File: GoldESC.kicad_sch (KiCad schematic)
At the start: 5 parts, among them U20 PSMN1R0-30YLDX

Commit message: Added fets and drivers, initial critical components selected
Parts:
- removed IC?: ESP32-S2, QFN56_ESP32_7X7_EXP, symbol AlfredoSymbols:ESP32-S2
- removed U20: PSMN1R0-30YLDX, Package_TO_SOT_SMD:LFPAK56, symbol AlfredoSymbols:PSMN1R0-30YLDX
- removed U?: LM5111-1M/NOPB, symbol AlfredoSymbols:LM5111-1M/NOPB
- removed U?: AD8417, symbol Amplifier_Current:AD8417
- removed U?: A4950E, Package_SO:SOIC-8-1EP_3.9x4.9mm_P1.27mm_EP2.41x3.3mm, symbol Driver_Motor:A4950E
- added C4: 470nF?/16V?, symbol Device:C_Small
- added C5, C6: ?uF/?V, symbol Device:C_Small
- added C? (x5): 2.2uF, Capacitor_SMD:C_0603_1608Metric, symbol Device:C
- added C? (x2): 100nF, Capacitor_SMD:C_0603_1608Metric, symbol Device:C
- added D1, D2, D3: S1M-13, Diode_SMD:D_SMA, symbol Diode:US1M
- added D?: GREEN, LED_THT:LED_D3.0mm, symbol Device:LED
- added D?: BLUE, LED_THT:LED_D3.0mm, symbol Device:LED
- added D?: ZMM3V3, Diode_SMD:D_MiniMELF, symbol Device:D_Zener
- added D?: RED, LED_THT:LED_D3.0mm, symbol Device:LED
- added J1: PhaseA, symbol Connector_Generic:Conn_01x01
- added J2: PhaseB, symbol Connector_Generic:Conn_01x01
- added J3: PhaseC, symbol Connector_Generic:Conn_01x01
- added J?: Conn_ESC_2A, Connector_PinSocket_2.54mm:PinSocket_1x11_P2.54mm_Vertical, symbol Connector_Generic:Conn_01x11
- added J? (x3): Conn_MCU_B, Connector_PinSocket_2.54mm:PinSocket_1x11_P2.54mm_Vertical, symbol Connector_Generic:Conn_01x11
- added J? (x4): Conn_01x06, Connector_PinSocket_2.54mm:PinSocket_1x06_P2.54mm_Vertical, symbol Connector_Generic:Conn_01x06
- added J?: Conn_MCU_A, Connector_PinSocket_2.54mm:PinSocket_1x11_P2.54mm_Vertical, symbol Connector_Generic:Conn_01x11
- added J?: Conn_ESC_1A, Connector_PinSocket_2.54mm:PinSocket_1x11_P2.54mm_Vertical, symbol Connector_Generic:Conn_01x11
- added R? (x4): 2K2, Resistor_SMD:R_0603_1608Metric, symbol Device:R
- added R? (x3): 3.3K, Resistor_SMD:R_0805_2012Metric, symbol Device:R
- added R? (x2): 22R, Resistor_SMD:R_0603_1608Metric, symbol Device:R
- added R? (x2): 10K, Resistor_SMD:R_0603_1608Metric, symbol Device:R
- added R?: 15K, Resistor_SMD:R_0603_1608Metric, symbol Device:R
- added R?: 10K RTC, Resistor_SMD:R_0603_1608Metric, symbol Device:R
- added U2: DRV8300NIPWR, Package_SO:TSSOP-20_4.4x6.5mm_P0.65mm, symbol AlfredoSymbols:DRV8300NIPWR
- added U3: MCP2551-I-SN, Package_SO:SOIC-8_3.9x4.9mm_P1.27mm, symbol Interface_CAN_LIN:MCP2551-I-SN
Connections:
- new net: D?.2 (A), R?.1 (x3)
- new net: C6.1, D3.1 (K), U2.14 (BSTC)
- new net: D1.2 (A), D2.2 (A), D3.2 (A), U2.7 (GVDD)
- new net: J?.5 (Pin_5), R?.2
- new net: C4.1, D1.1 (K), U2.20 (BSTA)
- new net: C5.1, D2.1 (K), U2.17 (BSTB)
- new net: J?.4 (Pin_4), R?.2
- new net +3V3: C?.1, C?.1, C?.1, C?.1, C?.1, J?.1 (Pin_1), J?.1 (Pin_1), J?.7 (Pin_7), J?.7 (Pin_7), J?.7 (Pin_7), R?.1, R?.1, R?.1, R?.1, R?.2, R?.2
- new net ADC_TEMP: J?.1 (Pin_1), J?.1 (Pin_1), J?.1 (Pin_1)
- new net D_CS: J?.2 (Pin_2)
- new net D_MISO: J?.4 (Pin_4)
- new net D_MOSI: J?.3 (Pin_3)
- new net D_SCK: J?.5 (Pin_5)
- new net EN_GATE: J?.8 (Pin_8), J?.8 (Pin_8), J?.8 (Pin_8)
- new net FAULT: J?.1 (Pin_1), J?.1 (Pin_1), J?.1 (Pin_1)
- new net FET_TEMP: R?.1, R?.2
- new net GE-Fets-A/GHx: U2.19 (GHA)
- new net GE-Fets-A/GLx: U2.11 (GLA)
- new net GE-Fets-A/PHx: J1.1 (Pin_1)
- new net GE-Fets-A/SHx: C4.2, U2.18 (SHA)
- new net GE-Fets-B/GHx: U2.16 (GHB)
- new net GE-Fets-B/GLx: U2.10 (GLB)
- new net GE-Fets-B/PHx: J2.1 (Pin_1)
- new net GE-Fets-B/SHx: C5.2, U2.15 (SHB)
- new net GE-Fets-C/GHx: U2.13 (GHC)
- new net GE-Fets-C/GLx: U2.9 (GLC)
- new net GE-Fets-C/PHx: J3.1 (Pin_1)
- new net GE-Fets-C/SHx: C6.2, U2.12 (SHC)
- new net GND: C?.1, C?.2, C?.2, C?.2, C?.2, C?.2, C?.2, D?.1 (K), D?.1 (K), D?.1 (K), D?.2 (A), J?.3 (Pin_3), J?.6 (Pin_6), J?.6 (Pin_6), J?.6 (Pin_6), J?.6 (Pin_6), J?.6 (Pin_6), J?.6 (Pin_6), R?.1, R?.2, U2.8 (GND)
- new net HALL_1: J?.3 (Pin_3), R?.2
- new net HALL_2: J?.4 (Pin_4), R?.2
- new net HALL_3: J?.5 (Pin_5), R?.2
- new net INH_A: J?.7 (Pin_7), J?.7 (Pin_7), J?.7 (Pin_7)
- new net INH_B: J?.5 (Pin_5), J?.5 (Pin_5), J?.5 (Pin_5)
- new net INH_C: J?.3 (Pin_3), J?.3 (Pin_3), J?.3 (Pin_3)
- new net INL_A: J?.6 (Pin_6), J?.6 (Pin_6), J?.6 (Pin_6)
- new net INL_B: J?.4 (Pin_4), J?.4 (Pin_4), J?.4 (Pin_4)
- new net INL_C: J?.2 (Pin_2), J?.2 (Pin_2), J?.2 (Pin_2)
- new net RX: J?.4 (Pin_4)
- new net S1_CS: J?.2 (Pin_2)
- new net S1_MISO_AE2: J?.1 (Pin_1), J?.4 (Pin_4)
- new net S1_MOSI: J?.5 (Pin_5)
- new net S1_SCK_AE1: J?.3 (Pin_3), J?.6 (Pin_6)
- new net S3_CS: J?.2 (Pin_2), J?.2 (Pin_2)
- new net S3_MISO: J?.4 (Pin_4), J?.4 (Pin_4)
- new net S3_MOSI: J?.3 (Pin_3), J?.3 (Pin_3)
- new net S3_SCK: J?.5 (Pin_5), J?.5 (Pin_5)
- new net SERVO: J?.1 (Pin_1)
- new net SH_A: J?.11 (Pin_11), J?.11 (Pin_11), J?.11 (Pin_11)
- new net SH_B: J?.10 (Pin_10), J?.10 (Pin_10), J?.10 (Pin_10)
- new net SH_C: J?.9 (Pin_9), J?.9 (Pin_9), J?.9 (Pin_9)
- new net SWCLK: J?.3 (Pin_3)
- new net SWDIO: J?.2 (Pin_2)
- new net TEMP_MOTOR: C?.2, J?.2 (Pin_2), R?.1
- new net TX: J?.5 (Pin_5)
- new net USB_DM: R?.1
- new net USB_DP: R?.1
- new net VDD: J?.8 (Pin_8), J?.8 (Pin_8), J?.8 (Pin_8), R?.2
- new net sCUR_A: J?.9 (Pin_9), J?.9 (Pin_9), J?.9 (Pin_9)
- new net sCUR_B: J?.10 (Pin_10), J?.10 (Pin_10), J?.10 (Pin_10)
- new net sCUR_C: J?.11 (Pin_11), J?.11 (Pin_11), J?.11 (Pin_11)
- new net sVLT_VDD: C?.1, D?.1 (K), R?.1, R?.2
- no-connect marks 0 -> 1
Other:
- added sheet GE-ESP32-S2 (GE-ESP32-S2.kicad_sch)
- added sheet GE-Fets-A (GE-Fets.kicad_sch)
- added sheet GE-Fets-B (GE-Fets.kicad_sch)
- added sheet GE-Fets-C (GE-Fets.kicad_sch)
- added sheet GE-Regs (GE-Regs.kicad_sch)
- note added: "Ref-map: 1 -39 -> fets/driver 40-69 -> Regs 70-89 -> ESP32 90-99 -> CAN"
- note added: "for VDDA"
- note added: "place next to VDD pins"

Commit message: switched to stm32
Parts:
- removed C? (x5): 2.2uF, Capacitor_SMD:C_0603_1608Metric, symbol Device:C
- removed J?: Conn_ESC_2A, Connector_PinSocket_2.54mm:PinSocket_1x11_P2.54mm_Vertical, symbol Connector_Generic:Conn_01x11
- removed J? (x3): Conn_MCU_B, Connector_PinSocket_2.54mm:PinSocket_1x11_P2.54mm_Vertical, symbol Connector_Generic:Conn_01x11
- removed J? (x4): Conn_01x06, Connector_PinSocket_2.54mm:PinSocket_1x06_P2.54mm_Vertical, symbol Connector_Generic:Conn_01x06
- removed J?: Conn_MCU_A, Connector_PinSocket_2.54mm:PinSocket_1x11_P2.54mm_Vertical, symbol Connector_Generic:Conn_01x11
- removed J?: Conn_ESC_1A, Connector_PinSocket_2.54mm:PinSocket_1x11_P2.54mm_Vertical, symbol Connector_Generic:Conn_01x11
- C5, C6: value ?uF/?V -> 470nF?/16V?
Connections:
- net GE-STM32F103/INHA: now reaches U2.1 (INHA)
- net GE-STM32F103/INHB: now reaches U2.2 (INHB)
- net GE-STM32F103/INHC: now reaches U2.3 (INHC)
- net GE-STM32F103/INLA: now reaches U2.4 (INLA)
- net GE-STM32F103/INLB: now reaches U2.5 (INLB)
- net GE-STM32F103/INLC: now reaches U2.6 (INLC)
- net FET_TEMP renamed TEMP_FETS
- no-connect marks 1 -> 0
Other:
- removed sheet GE-ESP32-S2
- added sheet GE-STM32F103 (GE-STM32F103.kicad_sch)
- note removed: "for VDDA"
- note removed: "place next to VDD pins"
- moved on the sheet: C?, D?, R?

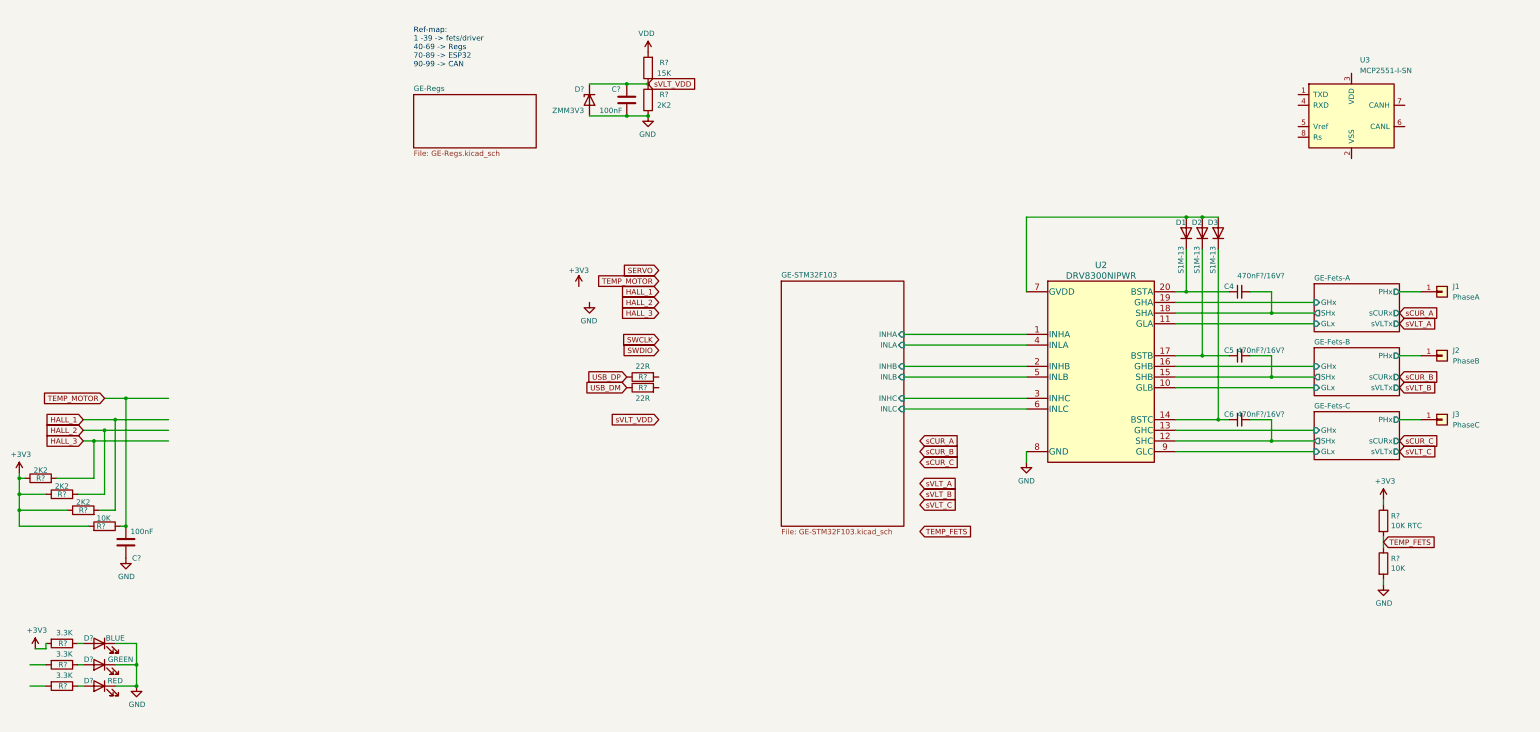
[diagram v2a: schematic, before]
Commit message: moved the Dsub off-board, most of initial layout routed
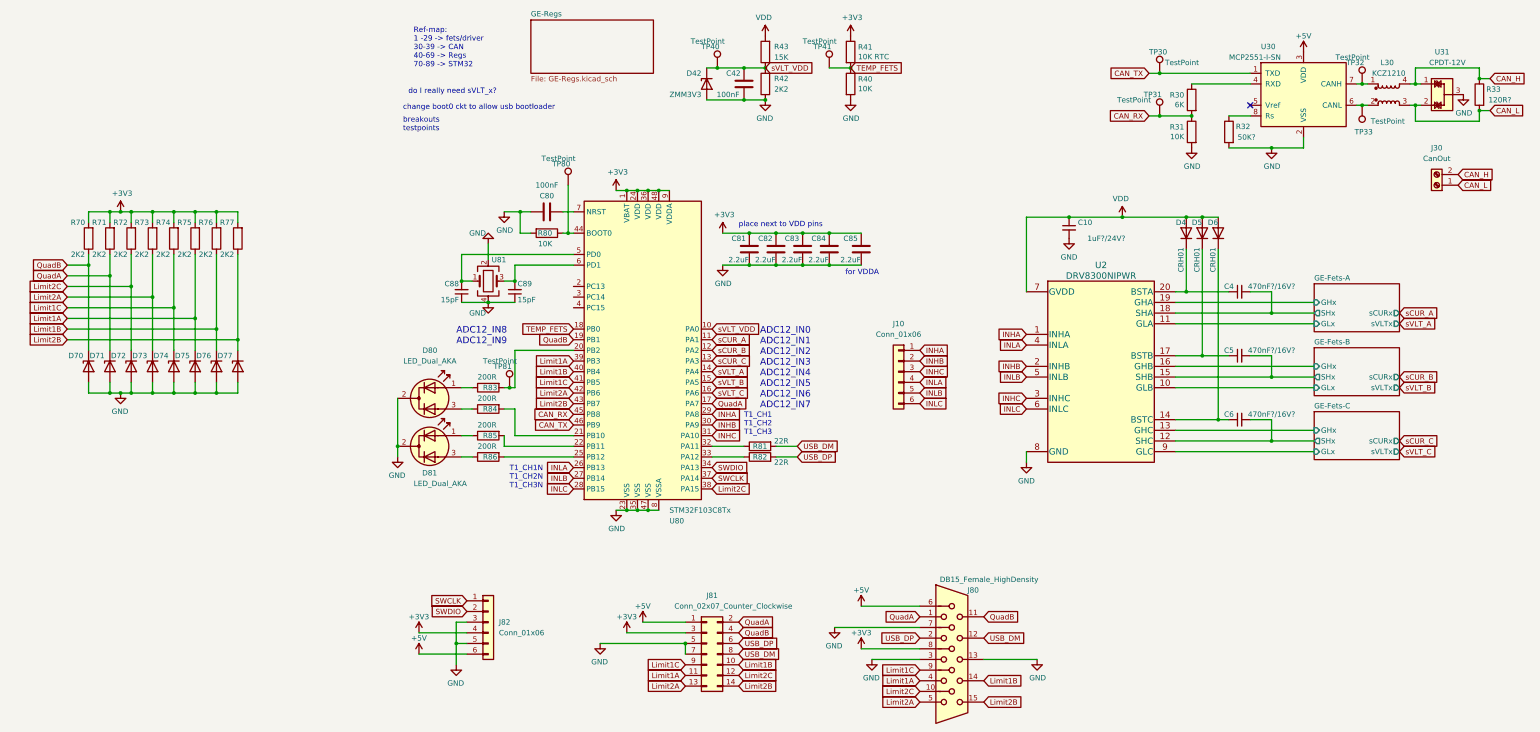
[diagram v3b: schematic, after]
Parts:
- removed C?: 100nF, Capacitor_SMD:C_0603_1608Metric, symbol Device:C
- removed D?: GREEN, LED_THT:LED_D3.0mm, symbol Device:LED
- removed D?: BLUE, LED_THT:LED_D3.0mm, symbol Device:LED
- removed D?: RED, LED_THT:LED_D3.0mm, symbol Device:LED
- removed J1: PhaseA, symbol Connector_Generic:Conn_01x01
- removed J2: PhaseB, symbol Connector_Generic:Conn_01x01
- removed J3: PhaseC, symbol Connector_Generic:Conn_01x01
- removed R? (x2): 3.3K, Resistor_SMD:R_0805_2012Metric, symbol Device:R
- removed R? (x3): 2K2, Resistor_SMD:R_0603_1608Metric, symbol Device:R
- removed R? (x2): 22R, Resistor_SMD:R_0603_1608Metric, symbol Device:R
- removed R?: 10K, Resistor_SMD:R_0603_1608Metric, symbol Device:R
- added C10: 1uF?/24V?, Capacitor_SMD:C_0805_2012Metric, symbol Device:C_Small
- added C80: 100nF, Capacitor_SMD:C_0603_1608Metric, symbol Device:C
- added C81, C82, C83, C84, C85: 2.2uF, Capacitor_SMD:C_0603_1608Metric, symbol Device:C
- added C88, C89: 15pF, Capacitor_SMD:C_0603_1608Metric, symbol Device:C_Small
- added D70, D71, D72, D73, D74, D75, D76, D77: Z3V3, Diode_SMD:D_MiniMELF, symbol Device:D_Zener
- added D80, D81: LED_Dual_AKA, LED_THT:LED_D3.0mm-3, symbol Device:LED_Dual_AKA
- added J10, J82: Conn_01x06, Connector_PinSocket_2.54mm:PinSocket_1x06_P2.54mm_Vertical, symbol Connector_Generic:Conn_01x06
- added J30: CanOut, AlfredoFootprints:TGD_ESC_SigPads, symbol Connector:Screw_Terminal_01x02
- added J80: DB15_Female_HighDensity, Connector_Dsub:DSUB-15-HD_Female_Horizontal_P2.29x1.98mm_EdgePinOffset3.03mm_Housed_MountingHolesOffset4.94mm, symbol Connector:DB15_Female_HighDensity
- added J81: Conn_02x07_Counter_Clockwise, Connector_IDC:IDC-Header_2x07_P2.54mm_Vertical, symbol Connector_Generic:Conn_02x07_Odd_Even
- added L30: KCZ1210, AlfredoFootprints:KCZ1210, symbol Device:L_Coupled_1423
- added R30: 6K, Resistor_SMD:R_0603_1608Metric, symbol Device:R
- added R31, R80: 10K, Resistor_SMD:R_0603_1608Metric, symbol Device:R
- added R32: 50K?, Resistor_THT:R_Axial_DIN0207_L6.3mm_D2.5mm_P10.16mm_Horizontal, symbol Device:R
- added R33: 120R?, Resistor_THT:R_Axial_DIN0207_L6.3mm_D2.5mm_P10.16mm_Horizontal, symbol Device:R
- added R70, R71, R72, R73, R74, R75, R76, R77: 2K2, Resistor_SMD:R_0603_1608Metric, symbol Device:R
- added R81, R82: 22R, Resistor_SMD:R_0603_1608Metric, symbol Device:R
- added R84, R85, R86: 200R, Resistor_SMD:R_0603_1608Metric, symbol Device:R
- added TP30, TP31, TP32, TP33, TP40, TP41, TP80, TP81: TestPoint, AlfredoFootprints:GE_TestPoint_Loop, symbol Connector:TestPoint
- added U31: CPDT-12V, Package_TO_SOT_SMD:SOT-23, symbol AlfredoSymbols:CPDT-12V
- added U80: STM32F103C8Tx, Package_QFP:LQFP-48_7x7mm_P0.5mm, symbol MCU_ST_STM32F1:STM32F103C8Tx
- added U81: Crystal_GND3, Crystal:Crystal_SMD_5032-4Pin_5.0x3.2mm, symbol Device:Crystal_GND24
- C4, C5, C6: footprint (none) -> Capacitor_SMD:C_0603_1608Metric; LCSC (none) -> ?
- D4: renamed from D1; value S1M-13 -> CRH01; footprint Diode_SMD:D_SMA -> Diode_SMD:D_SOD-123F
- D5: renamed from D2; value S1M-13 -> CRH01; footprint Diode_SMD:D_SMA -> Diode_SMD:D_SOD-123F
- D6: renamed from D3; value S1M-13 -> CRH01; footprint Diode_SMD:D_SMA -> Diode_SMD:D_SOD-123F
- R83: renamed from R?; value 3.3K -> 200R; footprint Resistor_SMD:R_0805_2012Metric -> Resistor_SMD:R_0603_1608Metric; LCSC C26010 -> ?
- U30: renamed from U3; LCSC (none) -> ?
- gave numbers to parts that had none: 6
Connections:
- net +3V3: now also C81.1, C82.1, C83.1, C84.1, C85.1, J80.8, J81.3 (Pin_3), J82.4 (Pin_4), R70.2, R71.2, R72.2, R73.2, R74.2, R75.2, R76.2, R77.2, U80.1 (VBAT), U80.24 (VDD), U80.36 (VDD), U80.48 (VDD), U80.9 (VDDA)
- net GND: now also U30.2 (VSS), C10.2, C80.2, C81.2, C82.2, C83.2, C84.2, C85.2, C88.1, C89.1, D70.2 (A), D71.2 (A), D72.2 (A), D73.2 (A), D74.2 (A), D75.2 (A), D76.2 (A), D77.2 (A), D80.2 (K), D81.2 (K), J80.13, J80.3, J80.7, J81.5 (Pin_5), J81.7 (Pin_7), J82.3 (Pin_3), J82.5 (Pin_5), R31.2, R32.2, R80.2, U31.3, U80.23 (VSS), U80.35 (VSS), U80.47 (VSS), U80.8 (VSSA), U81.2, U81.4
- net SWCLK: now also J82.1 (Pin_1), U80.37 (PA14)
- net SWDIO: now also J82.2 (Pin_2), U80.34 (PA13)
- net TEMP_FETS: now also TP41.1, U80.18 (PB0)
- net USB_DM: now also J80.12, J81.8 (Pin_8), R81.2
- net USB_DP: now also J80.2, J81.6 (Pin_6), R82.2
- net VDD: now also D4.2 (A), D5.2 (A), D6.2 (A), U2.7 (GVDD), C10.1
- net sCUR_A: now also U80.11 (PA1)
- net sCUR_B: now also U80.12 (PA2)
- net sCUR_C: now also U80.13 (PA3)
- net sVLT_A: now also U80.14 (PA4)
- net sVLT_B: now also U80.15 (PA5)
- net sVLT_C: now also U80.16 (PA6)
- net sVLT_VDD: now also TP40.1, U80.10 (PA0)
- net at R83.1: now also D80.1 (A1)
- net at R83.2: now also TP81.1, U80.20 (PB2)
- net CAN_TX: now reaches U30.1 (TXD)
- net CAN_TX: now also TP30.1, U80.46 (PB9)
- net +5V: now reaches U30.3 (VDD)
- net +5V: now also J80.6, J81.1 (Pin_1), J82.6 (Pin_6)
- net at U30.4 (RXD): now also R30.1
- net at U30.6 (CANL): now also L30.2, TP33.1
- net at U30.7 (CANH): now also L30.1, TP32.1
- net at U30.8 (Rs): now also R32.1
- net GE-STM32F103/INHA renamed INHA
- net INHA: now also J10.1 (Pin_1), U80.29 (PA8)
- net GE-STM32F103/INHB renamed INHB
- net INHB: now also J10.2 (Pin_2), U80.30 (PA9)
- net GE-STM32F103/INHC renamed INHC
- net INHC: now also J10.3 (Pin_3), U80.31 (PA10)
- net GE-STM32F103/INLA renamed INLA
- net INLA: now also J10.4 (Pin_4), U80.26 (PB13)
- net GE-STM32F103/INLB renamed INLB
- net INLB: now also J10.5 (Pin_5), U80.27 (PB14)
- net GE-STM32F103/INLC renamed INLC
- net INLC: now also J10.6 (Pin_6), U80.28 (PB15)
- new net: C89.2, U80.6 (PD1), U81.3
- new net: C88.2, U80.5 (PD0), U81.1
- new net: R80.1, TP80.1, U80.44 (BOOT0)
- new net: D80.3 (A2), R84.1
- new net: D81.3 (A2), R86.1
- new net: R86.2, U80.25 (PB12)
- new net: R84.2, U80.21 (PB10)
- new net: R85.2, U80.22 (PB11)
- new net: R81.1, U80.32 (PA11)
- new net: R82.1, U80.33 (PA12)
- new net: C80.1, U80.7 (NRST)
- new net: D81.1 (A1), R85.1
- new net CAN_H: J30.2 (Pin_2), L30.4, R33.1, U31.1
- new net CAN_L: J30.1 (Pin_1), L30.3, R33.2, U31.2
- new net CAN_RX: R30.2, R31.1, TP31.1, U80.45 (PB8)
- new net Limit1A: D75.1 (K), J80.4, J81.11 (Pin_11), R75.1, U80.39 (PB3)
- new net Limit1B: D76.1 (K), J80.14, J81.10 (Pin_10), R76.1, U80.40 (PB4)
- new net Limit1C: D74.1 (K), J80.9, J81.9 (Pin_9), R74.1, U80.41 (PB5)
- new net Limit2A: D73.1 (K), J80.5, J81.13 (Pin_13), R73.1, U80.42 (PB6)
- new net Limit2B: D77.1 (K), J80.15, J81.14 (Pin_14), R77.1, U80.43 (PB7)
- new net Limit2C: D72.1 (K), J80.10, J81.12 (Pin_12), R72.1, U80.38 (PA15)
- new net QuadA: D71.1 (K), J80.1, J81.2 (Pin_2), R71.1, U80.17 (PA7)
- new net QuadB: D70.1 (K), J80.11, J81.4 (Pin_4), R70.1, U80.19 (PB1)
- no-connect marks 0 -> 1
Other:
- removed sheet GE-STM32F103
- sheet GE-Fets-A ports: added none; removed PHx
- sheet GE-Fets-B ports: added none; removed PHx
- sheet GE-Fets-C ports: added none; removed PHx
- note added: "ADC12_IN0 ADC12_IN1 ADC12_IN2 ADC12_IN3 ADC12_IN4 ADC12_IN5 ADC12_IN6 ADC12_IN7"
- note added: "ADC12_IN8 ADC12_IN9"
- note added: "Ref-map: 1 -29 -> fets/driver 30-39 -> CAN 40-69 -> Regs 70-89 -> STM32"
- note added: "T1_CH1 T1_CH2 T1_CH3"
- note added: "T1_CH1N T1_CH2N T1_CH3N"
- note added: "breakouts testpoints"
- note added: "change boot0 ckt to allow usb bootloader"
- note added: "do I really need sVLT_x?"
- note added: "for VDDA"
- note added: "place next to VDD pins"
- note removed: "Ref-map: 1 -39 -> fets/driver 40-69 -> Regs 70-89 -> ESP32 90-99 -> CAN"
- moved on the sheet: C42, D42, R40, R41, R42, R43, R83, U30

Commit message: Updated BOM
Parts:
- C10: value 1uF?/24V? -> 1uF
- C4, C5, C6: value 470nF?/16V? -> 1uF; LCSC ? -> C15849
- D4, D5, D6: LCSC (none) -> C845528
- R30: value 6K -> 5.6K; LCSC ? -> C23189
- R83, R84, R85, R86: LCSC ? -> C8218
- U30: LCSC ? -> C7376
- U80: LCSC ? -> C8734
